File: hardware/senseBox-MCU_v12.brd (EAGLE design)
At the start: 86 x 66 mm, 140 parts, among them IC1 VREG-AP2111H-3V3, IC2 ATSAMD21G18A-MU, IC3 MAX8XX-809R, IC4 MAX8XX-809R, IC5 74LVC244PW, IC6 BMX055, IC7 ATECC608A-MAHDA, J1 USB-MICROB-2, J10 JST4-B4B-PH-SM4-TB, J11 JST4-B4B-PH-SM4-TB, J12 JST4-B4B-PH-SM4-TB, J13 JST4-B4B-PH-SM4-TB, J14 JUMPER3-0402, J15 JUMPER3-0402, J2 JST2-B2B-PH-SM4-TB, J3 SWD-2X5-SMD, J4 JST4-B4B-PH-SM4-TB, J5 JST4-B4B-PH-SM4-TB, J6 JST4-B4B-PH-SM4-TB, J7 JST4-B4B-PH-SM4-TB, J8 JST4-B4B-PH-SM4-TB, J9 JST4-B4B-PH-SM4-TB, Q1 32.768KHz, SW1 PTS645SH50SMTR92-Grey, SW2 PTS645SK50SMTR92-Red, T1 BSS138PS, T2 P-Chn, T3 P-Chn, T4 P-Chn, T5 BSS138PS, T6 BSS138PS, T7 P-Chn, X1 PASSER-07, X2 PASSER-07, X3 PASSER-07, X4 PASSER-07

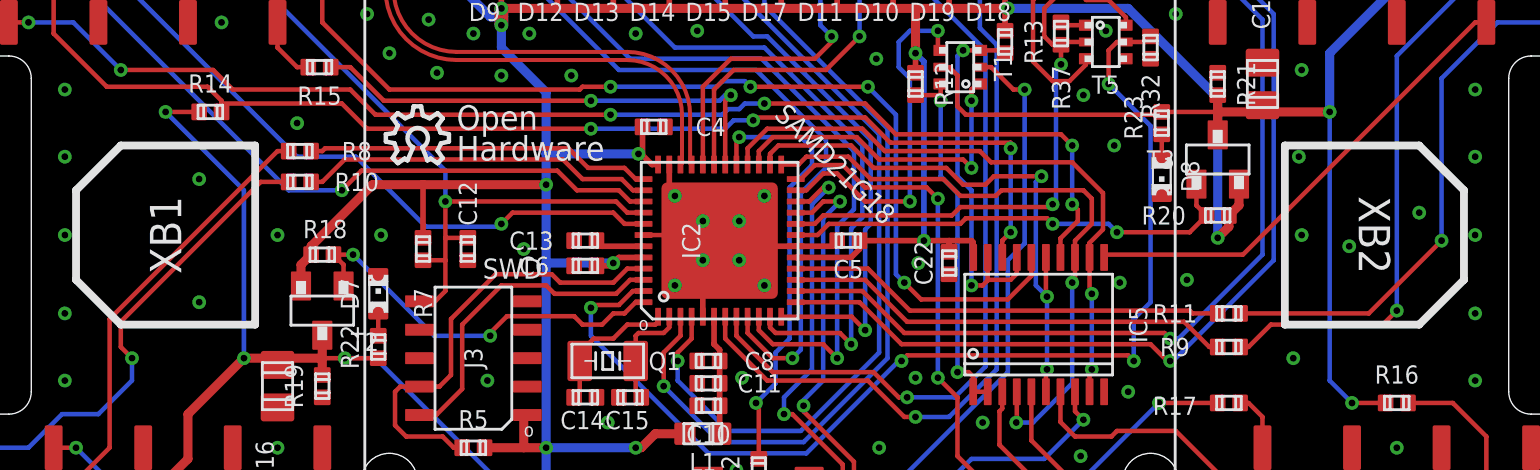
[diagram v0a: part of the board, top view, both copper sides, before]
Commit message: updated schematics
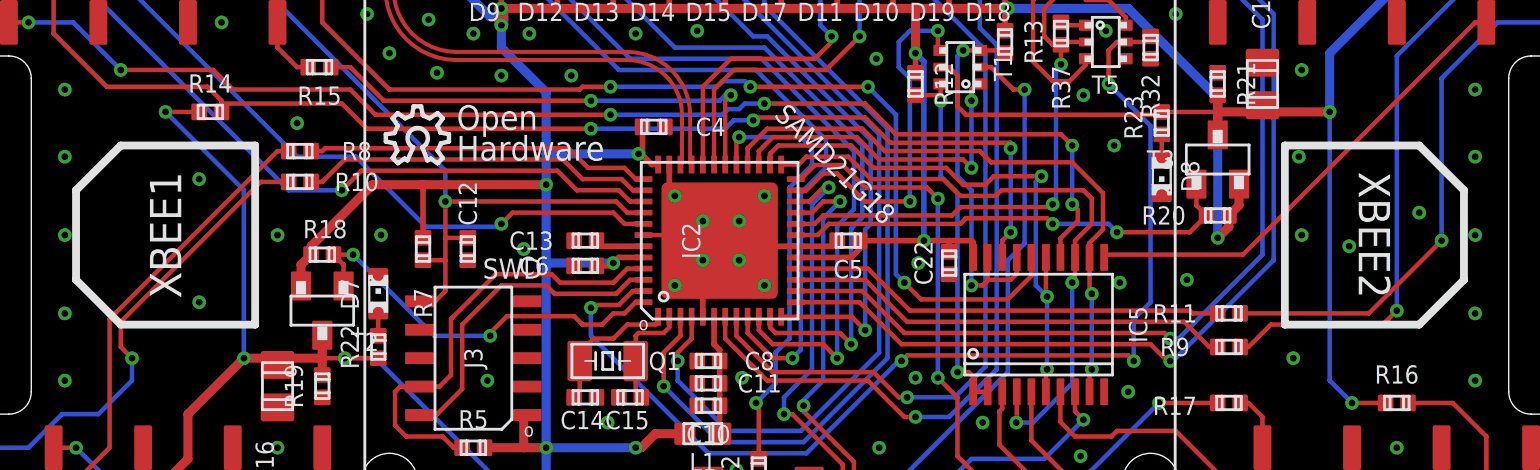
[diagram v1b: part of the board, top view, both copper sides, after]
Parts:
- renumbered XB1 to XBEE1, XB2 to XBEE2
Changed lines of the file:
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@@
 <element name="X3" library="we-symbol" package="PASSER_07MM" value="PASSER-07" x="84" y="64" smashed="yes"/>
 <element name="LOGO3" library="we-symbol" package="OSHW_3MM" value="OSHW_LOGOX0070" x="27.25" y="25.5" smashed="yes"/>
-<element name="XB1" library="we-board" package="XBEE_SMD_TP" value="XBEE-SMDTP" x="14" y="21" smashed="yes" rot="R90">
+<element name="XBEE1" library="we-board" package="XBEE_SMD_TP" value="XBEE-SMDTP" x="14" y="21" smashed="yes" rot="R90">
 <attribute name="NAME" x="16" y="21" size="1.4" layer="21" font="vector" ratio="14" rot="SR90" align="center"/>
 <attribute name="VALUE" x="15.27" y="21" size="0.8128" layer="27" font="vector" ratio="10" rot="R270" align="center"/>
@@
 <attribute name="VALUE" x="19.4125" y="14.25" size="0.8128" layer="27" font="vector" ratio="10" rot="R90" align="center"/>
 </element>
-<element name="XB2" library="we-board" package="XBEE_SMD_TP" value="XBEE-SMDTP" x="72" y="21" smashed="yes" rot="R270">
+<element name="XBEE2" library="we-board" package="XBEE_SMD_TP" value="XBEE-SMDTP" x="72" y="21" smashed="yes" rot="R270">
 <attribute name="NAME" x="70" y="21" size="1.4" layer="21" font="vector" ratio="14" rot="SR270" align="center"/>
 <attribute name="VALUE" x="70.73" y="21" size="0.8128" layer="27" font="vector" ratio="10" rot="R90" align="center"/>
@@
 <vertex x="0" y="5"/>
 </polygon>
-<contactref element="XB1" pad="10"/>
+<contactref element="XBEE1" pad="10"/>
 <contactref element="IC2" pad="TP"/>
 <contactref element="IC2" pad="18"/>
@@
 <contactref element="C7" pad="1"/>
 <contactref element="C3" pad="1"/>
-<contactref element="XB2" pad="10"/>
+<contactref element="XBEE2" pad="10"/>
 <contactref element="C20" pad="1"/>
 <contactref element="C18" pad="1"/>
@@
 </signal>
 <signal name="XB1_VCC">
-<contactref element="XB1" pad="1"/>
+<contactref element="XBEE1" pad="1"/>
 <contactref element="C20" pad="2"/>
 <contactref element="C18" pad="2"/>
@@
 </signal>
 <signal name="XB1_TX">
-<contactref element="XB1" pad="2"/>
+<contactref element="XBEE1" pad="2"/>
 <contactref element="R10" pad="2"/>
 <wire x1="7" y1="11.5" x2="8" y2="11.5" width="0.2032" layer="1"/>
@@
 </signal>
 <signal name="XB1_MISO">
-<contactref element="XB1" pad="4"/>
+<contactref element="XBEE1" pad="4"/>
 <contactref element="IC5" pad="8"/>
 <via x="57" y="12.75" extent="1-16" drill="0.3"/>
@@
 </signal>
 <signal name="XB1_RX">
-<contactref element="XB1" pad="3"/>
+<contactref element="XBEE1" pad="3"/>
 <contactref element="R8" pad="2"/>
 <wire x1="9" y1="8.5" x2="10.5" y2="8.5" width="0.2032" layer="1"/>
@@
 </signal>
 <signal name="XB1_CS">
-<contactref element="XB1" pad="17"/>
+<contactref element="XBEE1" pad="17"/>
 <contactref element="IC5" pad="18"/>
 <contactref element="R14" pad="1"/>
@@
 </signal>
 <signal name="XB1_MOSI">
-<contactref element="XB1" pad="11"/>
+<contactref element="XBEE1" pad="11"/>
 <contactref element="IC5" pad="16"/>
 <wire x1="26" y1="27.5" x2="34.5" y2="27.5" width="0.2032" layer="1"/>
@@
 </signal>
 <signal name="XB1_SCK">
-<contactref element="XB1" pad="18"/>
+<contactref element="XBEE1" pad="18"/>
 <contactref element="IC5" pad="14"/>
 <wire x1="25.375" y1="26.375" x2="35.875" y2="26.375" width="0.2032" layer="1"/>
@@
 </signal>
 <signal name="XBEE1_CTS/IRQ">
-<contactref element="XB1" pad="12"/>
+<contactref element="XBEE1" pad="12"/>
 <contactref element="R15" pad="1"/>
 <wire x1="21" y1="30.5" x2="21" y2="29.375" width="0.2032" layer="1"/>
@@
 </signal>
 <signal name="XB2_VCC">
-<contactref element="XB2" pad="1"/>
+<contactref element="XBEE2" pad="1"/>
 <contactref element="C17" pad="2"/>
 <contactref element="C19" pad="2"/>
@@
 </signal>
 <signal name="XB2_TX">
-<contactref element="XB2" pad="2"/>
+<contactref element="XBEE2" pad="2"/>
 <contactref element="R11" pad="2"/>
 <wire x1="79" y1="30.5" x2="78" y2="30.5" width="0.2032" layer="1"/>
@@
 </signal>
 <signal name="XB2_RX">
-<contactref element="XB2" pad="3"/>
+<contactref element="XBEE2" pad="3"/>
 <contactref element="R9" pad="2"/>
 <wire x1="77" y1="33.5" x2="76" y2="33.5" width="0.2032" layer="1"/>
@@
 </signal>
 <signal name="XB2_MISO">
-<contactref element="XB2" pad="4"/>
+<contactref element="XBEE2" pad="4"/>
 <contactref element="IC5" pad="11"/>
 <wire x1="75" y1="30.5" x2="74.5" y2="30.5" width="0.2032" layer="1"/>
@@
 </signal>
 <signal name="XB2_SCK">
-<contactref element="XB2" pad="18"/>
+<contactref element="XBEE2" pad="18"/>
 <contactref element="IC5" pad="5"/>
 <wire x1="77" y1="11.5" x2="77" y2="9" width="0.2032" layer="1"/>
@@
 </signal>
 <signal name="XB2_CS">
-<contactref element="XB2" pad="17"/>
+<contactref element="XBEE2" pad="17"/>
 <contactref element="R16" pad="1"/>
 <contactref element="IC5" pad="3"/>
@@
 </signal>
 <signal name="XBEE2_CTS/IRQ">
-<contactref element="XB2" pad="12"/>
+<contactref element="XBEE2" pad="12"/>
 <contactref element="R17" pad="1"/>
 <wire x1="65" y1="11.5" x2="65" y2="12.875" width="0.2032" layer="1"/>
@@
 </signal>
 <signal name="XB2_MOSI">
-<contactref element="XB2" pad="11"/>
+<contactref element="XBEE2" pad="11"/>
 <contactref element="IC5" pad="7"/>
 <wire x1="55.975" y1="14" x2="55.975" y2="12.65" width="0.2032" layer="1"/>
@@
 </signal>
 <signal name="RST_XB1">
-<contactref element="XB1" pad="5"/>
+<contactref element="XBEE1" pad="5"/>
 <contactref element="IC4" pad="2"/>
 <wire x1="13" y1="8.5" x2="13" y2="6.6" width="0.2032" layer="1"/>
@@
 </signal>
 <signal name="RST_XB2">
-<contactref element="XB2" pad="5"/>
+<contactref element="XBEE2" pad="5"/>
 <contactref element="IC3" pad="2"/>
 <wire x1="68.9" y1="36.05" x2="69.075" y2="36.05" width="0.2032" layer="1"/>
